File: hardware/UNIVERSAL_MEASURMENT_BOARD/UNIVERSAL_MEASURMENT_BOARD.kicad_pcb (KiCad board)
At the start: 6 copper layers, 75 x 95 mm, 198 parts, among them J1 2606-1110_010-000, J2 2606-1110_010-000, J3 2606-1110_010-000, J4 2606-1110_010-000, J5 Strain Relief, J6 Strain Relief, J7 FTSH-107-01-L-D-K, J8 Strain Relief, J9 Strain Relief, U1 ADS8863IDGS, U10 LT3471EDD#PBF, U11 L7812ABD2T-TR, U12 ISL21010CFH330Z-TK, U13 L78L15ACD13TR, U14 TPS54202HDDCR, U15 L79L15ACD13TR, U16 ADM3057EBRWZ, U2 STM32G484RET3, U3 PGA280AIPW, U4 CD4097BM, U5 UA78M33CDCYRG3, U6 TPS54202HDDCR, U7 UA78M33CDCYRG3, U8 L7805ABD2T-TR, U9 ISL21010CFH315Z-TK, Y1 ATX-H11-F-16.000MHz-G100-T

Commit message: Finish PCB routing
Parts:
- removed the REF** at (109.3, 53.4)
- removed the REF** at (39.8, 128.4)
- removed the REF** at (109.3, 128.9) (x2)
- removed the REF** at (39.8, 52.9) (x2)
- removed the REF** at (109.3, 52.9)
- removed the REF** at (39.8, 128.9)
- removed TP1: M15V, REST:TestPoint_Pad_D1.5mm
- removed TP10: 15VA, REST:TestPoint_Pad_D1.5mm
- removed TP11: 7V, REST:TestPoint_Pad_D1.5mm
- removed TP12: -15VA, REST:TestPoint_Pad_D1.5mm
- removed TP13: CVISO, REST:TestPoint_Pad_D1.5mm
- removed TP2: 3V3, REST:TestPoint_Pad_D1.5mm
- removed TP3: 3V3A, REST:TestPoint_Pad_D1.5mm
- removed TP4: 18V, REST:TestPoint_Pad_D1.5mm
- removed TP5: 5VA, REST:TestPoint_Pad_D1.5mm
- removed TP6: 1V5A, REST:TestPoint_Pad_D1.5mm
- removed TP7: 12VA, REST:TestPoint_Pad_D1.5mm
- removed TP8: -18V, REST:TestPoint_Pad_D1.5mm
- removed TP9: 3V0A, REST:TestPoint_Pad_D1.5mm
- moved R13 22.8 mm to (65.4, 57.4), turned to 90 degrees
- moved C2 4.43 mm to (77.3, 118.1), turned to 90 degrees
- moved C3 3.48 mm to (77.3, 121.4), turned to -90 degrees
- moved C67 3.44 mm to (61.1, 82.9), turned to 90 degrees
- moved F2 2.68 mm to (66.1, 55.0), turned to 0 degrees
- moved C1 1.80 mm to (71.4, 122.2)
- moved C4 1.80 mm to (74.7, 122.2)
- moved U1 1.80 mm to (73.0, 119.6)
- moved C40 1.66 mm to (67.0, 57.4)
- moved C29 1.52 mm to (71.6, 94.7), turned to -90 degrees
- moved C44 1.28 mm to (66.2, 49.0)
- moved R11 1.28 mm to (66.2, 52.2)
- moved C31 1.00 mm to (68.0, 97.4), turned to 90 degrees
- moved U9 0.57 mm to (62.7, 96.1)
- moved C45 0.53 mm to (64.6, 49.0)
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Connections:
- REF** pad 1: GND -> (no net) (x4)
- U2 pad 33: /mcu & adc/ADDR1 -> /can/CAN_STB
- U2 pad 34: /mcu & adc/ADDR2 -> /can/CAN_TX
- U2 pad 35: /mcu & adc/MUXEN -> /can/CAN_RX
- U2 pad 36: /mcu & adc/ADDR3 -> unconnected-(U2-PB14-Pad36)
- U2 pad 43: unconnected-(U2-PA9-Pad43) -> /mcu & adc/ADDR1
- U2 pad 44: unconnected-(U2-PA10-Pad44) -> /mcu & adc/ADDR2
- U2 pad 45: /can/CAN_TX -> /mcu & adc/ADDR3
- U2 pad 46: /can/CAN_RX -> /mcu & adc/MUXEN
- U2 pad 51: /can/CAN_STB -> unconnected-(U2-PA15-Pad51)
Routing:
- net +5V0A: track 1.48 -> 239.9 mm, vias 0 -> 12
- net +12V0A: track 0.00 -> 209.9 mm, vias 0 -> 12
- net +3V3: track 12.0 -> 191.4 mm, vias 1 -> 10
- net /connectors/A1N: track 3.53 -> 139.0 mm, vias 0 -> 3
- net /connectors/A8P: track 3.52 -> 122.9 mm, vias 0 -> 1
- net /connectors/A1P: track 3.07 -> 117.9 mm, vias 0 -> 1
- net /connectors/A2N: track 3.89 -> 117.8 mm, vias 0 -> 3
- net /connectors/A7P: track 3.16 -> 100.9 mm, vias 0 -> 1
- net /connectors/A8N: track 3.98 -> 101.7 mm, vias 0 -> 1
- net /connectors/A2P: track 3.43 -> 99.5 mm, vias 0 -> 1
- net /connectors/A3N: track 3.63 -> 94.8 mm, vias 0 -> 3
- net +14V0: track 3.48 -> 85.2 mm, vias 8 -> 11
- net /connectors/A7N: track 3.63 -> 82.9 mm, vias 0 -> 1
- net /can/CAN_RX: track 5.84 -> 84.5 mm, vias 1 -> 2
- net /connectors/A3P: track 3.16 -> 79.0 mm, vias 0 -> 1
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- added copper zone on In2.Cu, net GND_ISO
- added copper zone on In3.Cu, net GND_ISO
- added copper zone on In4.Cu, net GND_ISO
- added copper zone on F.Cu, net Net-(D1-A)
- added copper zone on F.Cu, net Net-(U10-SW2)
- added copper zone on In1.Cu, net Net-(U14-SW)
- added copper zone on In1.Cu, net Net-(U6-SW)
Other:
- board text added: "U15"
- board text removed: "U7"

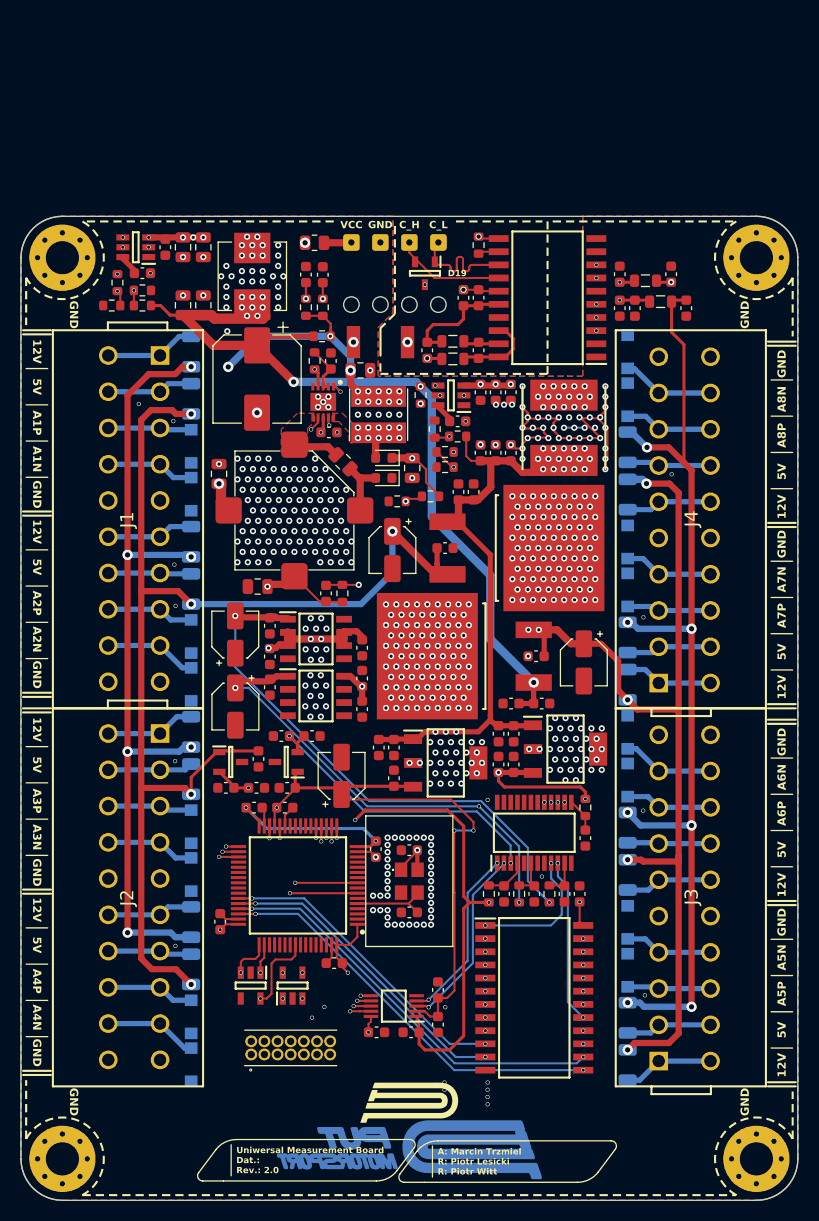
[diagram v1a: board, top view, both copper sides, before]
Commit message: Solved ERC & DRC
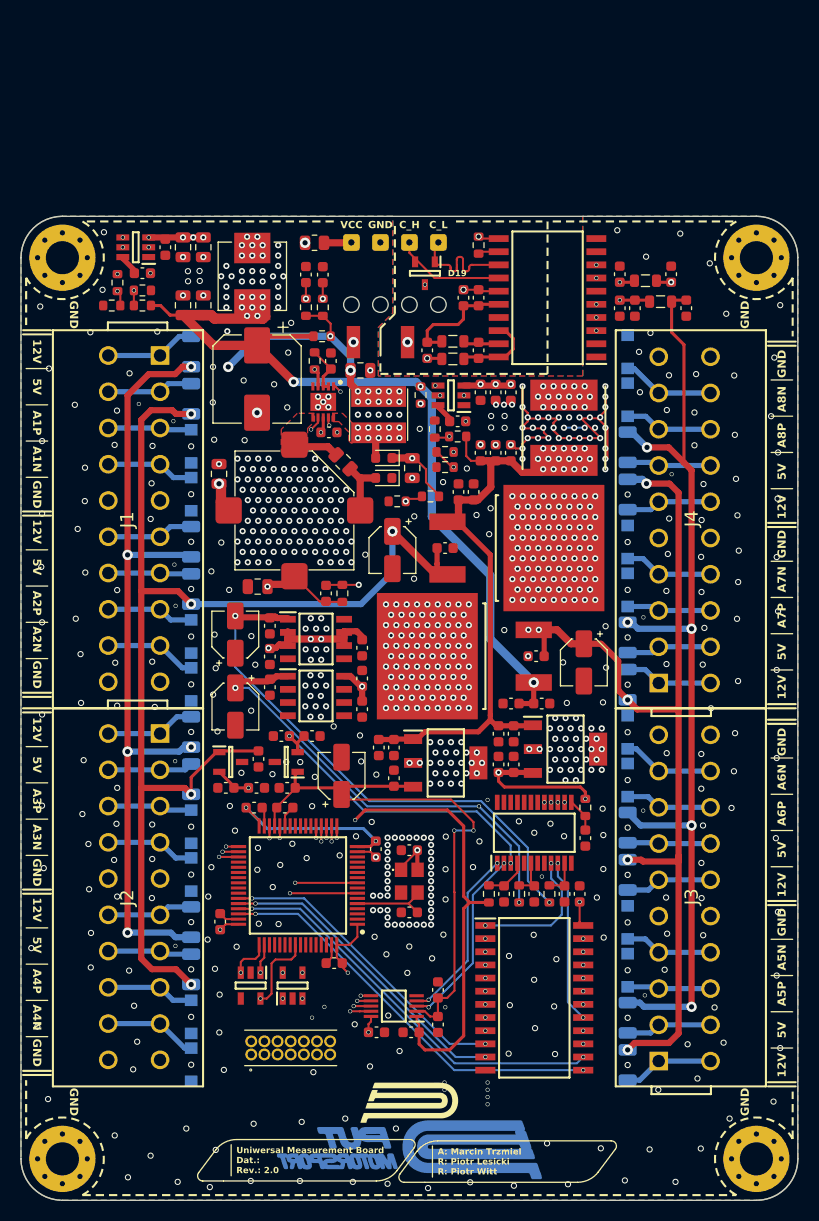
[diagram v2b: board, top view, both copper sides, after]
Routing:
- net Net-(U6-SW): track 15.2 -> 12.6 mm
- net +14V0F: track 45.3 -> 44.4 mm
- net GND: vias 517 -> 790
- net +7V0: vias 19 -> 16
- net +5V0A: vias 12 -> 10
- net +3V3A: vias 3 -> 2
- net +3V0A: vias 4 -> 3
- net +12V0A: vias 12 -> 11

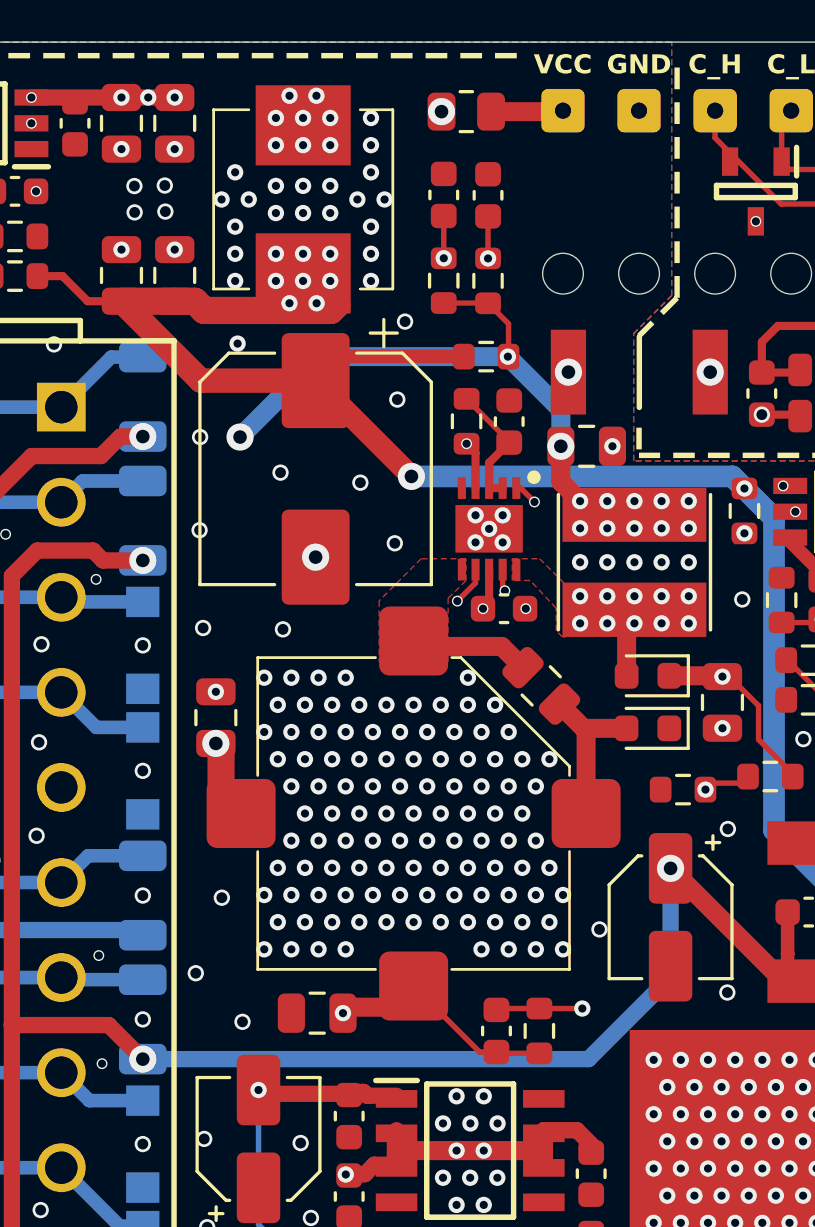
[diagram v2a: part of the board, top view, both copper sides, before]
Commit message: Review fix: rework feedback circuit of -18V converter
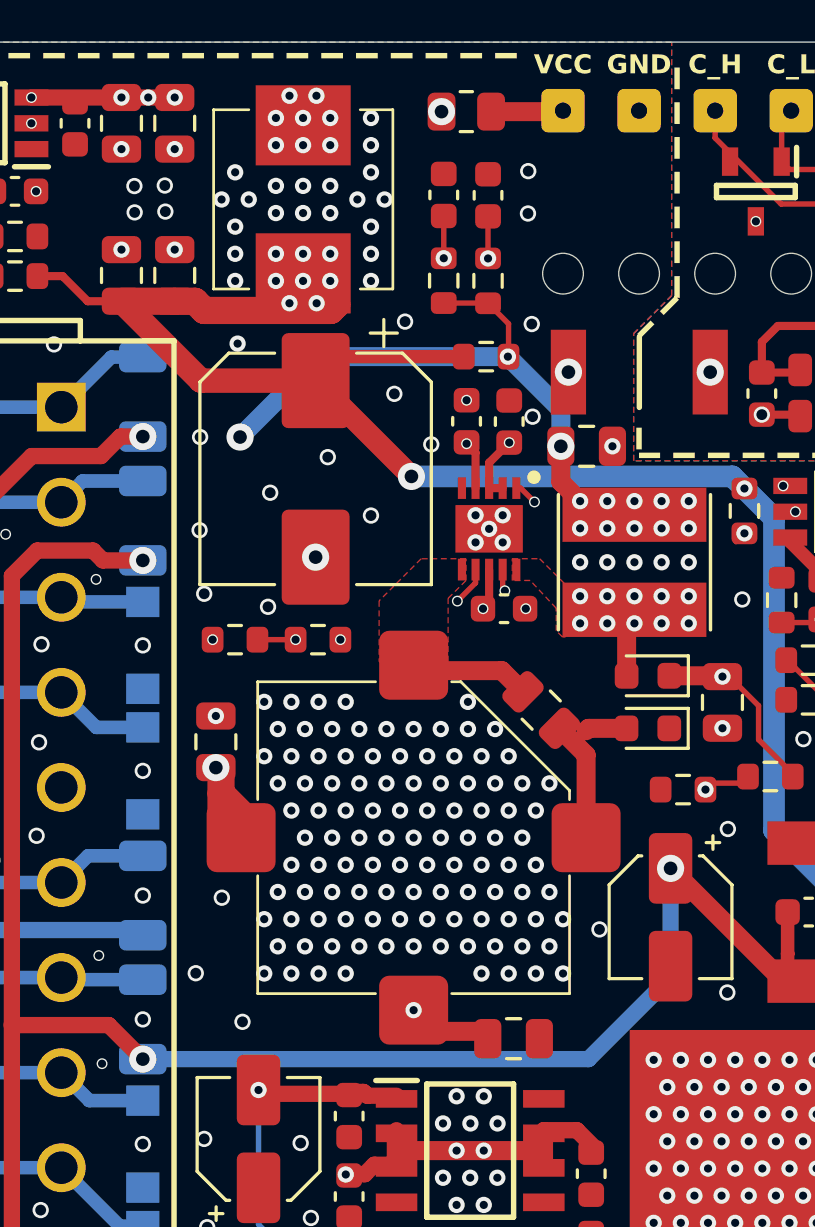
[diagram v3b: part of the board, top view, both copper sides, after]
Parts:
- moved C46 22.5 mm to (65.4, 57.4), turned to -90 degrees
- moved R14 18.2 mm to (56.9, 65.4), turned to 0 degrees
- moved R13 9.72 mm to (59.9, 65.4), turned to 0 degrees
- moved C53 7.29 mm to (67.1, 80.1), turned to 180 degrees
- moved C51 0.89 mm to (68.1, 68.0)
- moved C52 0.89 mm to (56.2, 69.2)
- moved L3 0.89 mm to (63.5, 72.7)
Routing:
- net -18V0: track 27.8 -> 59.4 mm, vias 4 -> 6
- net Net-(U10-FB2P): track 28.0 -> 13.0 mm
- net Net-(U10-FB1P): track 4.74 -> 12.3 mm, vias 0 -> 2
- net +14V0F: track 44.4 -> 45.3 mm
- net GND: vias 790 -> 795
